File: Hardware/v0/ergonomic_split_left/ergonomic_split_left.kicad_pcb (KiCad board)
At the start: 2 copper layers, 182.6 x 172.4 mm, 96 parts, among them J1 USB_C_Receptacle_USB2.0, J2 Right_Interface, J3 Conn_01x02_Male, J5 Conn_02x03_Odd_Even, SW1 SW_Push, SW10 L31, SW11 L41, SW12 L51, SW13 L02, SW14 L12, SW15 L22, SW16 L32, SW17 L42, SW18 L52, SW19 L03, SW2 L00, SW20 L13, SW21 L23, SW22 L33, SW23 L43, SW24 L53, SW25 L04, SW26 L14, SW27 L24, SW28 L34, SW29 L44, SW3 L10, SW30 L54, SW31 L05, SW32 L15, SW33 L25, SW34 L35, SW35 L55, SW36 L16, SW37 L36, SW38 L56, SW39 L06, SW4 L20, SW40 L_Encoder, SW5 L30, SW6 L40, SW7 L01, SW8 L11, SW9 L21, U1 SRV05-4, U2 PCAL9555AHF, U6 ATmega32U4-AU, U9 TCR2EF33, X2 KC2016K

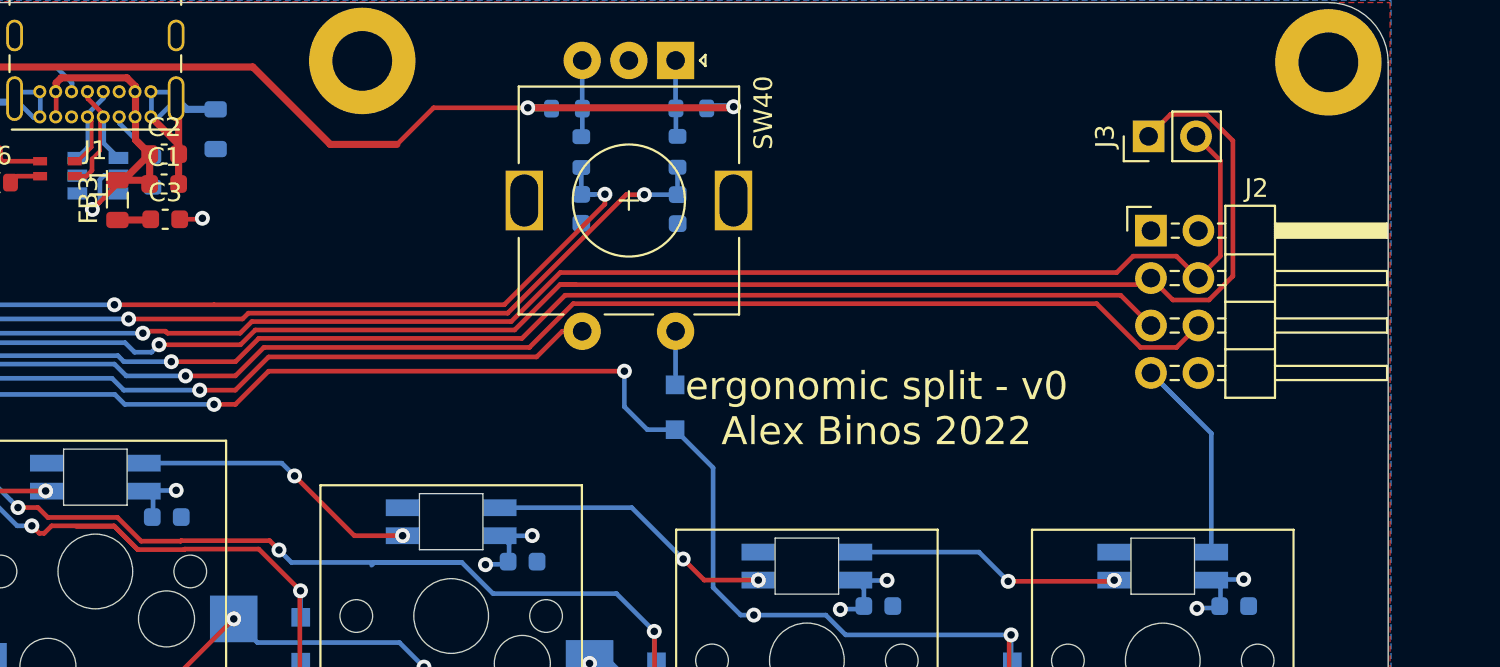
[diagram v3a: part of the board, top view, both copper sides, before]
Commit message: Moving right interface connector
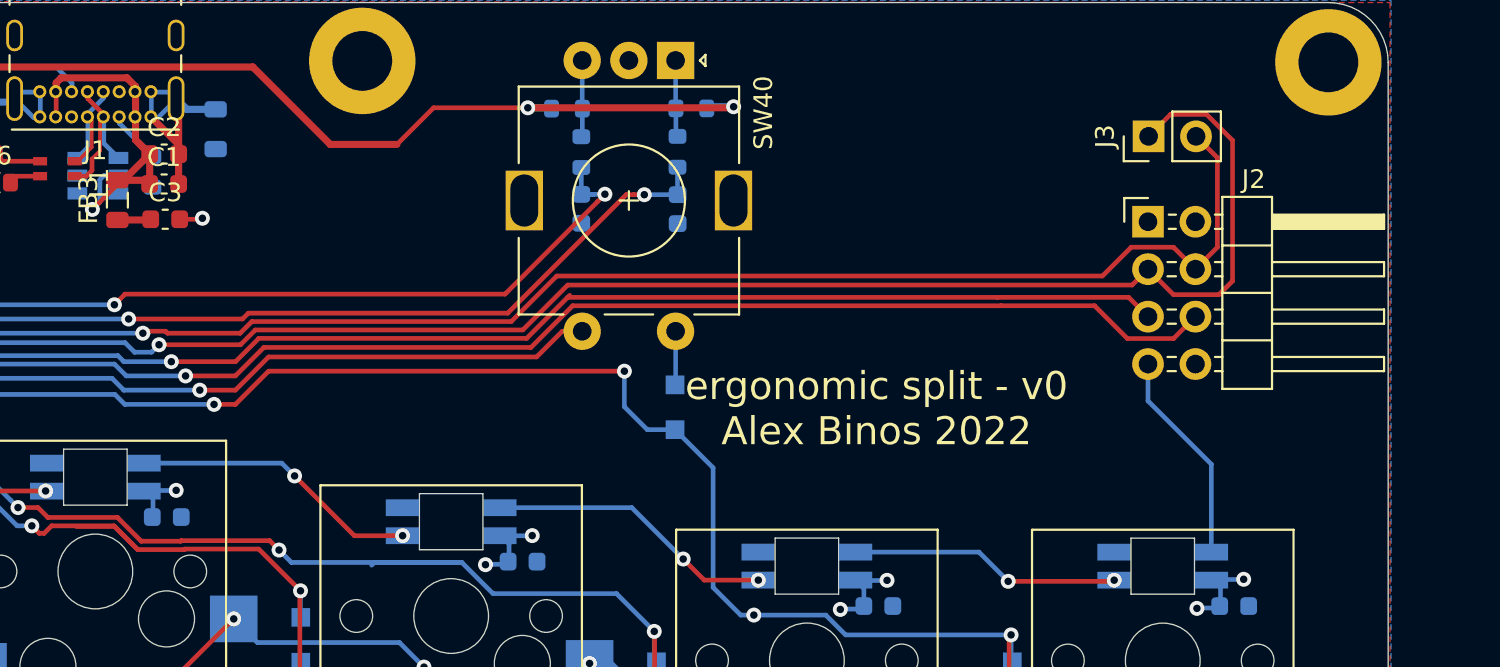
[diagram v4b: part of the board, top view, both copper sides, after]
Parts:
- moved J2 0.50 mm to (211.9, 65.4)
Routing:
- net /Right Interface/RGB_DIN: track 14.0 -> 11.5 mm
- net /IO Expander/SDA: track 137.5 -> 136.9 mm
- net /IO Expander/SCL: track 128.1 -> 127.6 mm
